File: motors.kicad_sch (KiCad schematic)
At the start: 0 parts

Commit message: Ajout des deux moteurs
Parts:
- added C12, C17: 1µF, Capacitor_SMD:C_0805_2012Metric, symbol local:C_0402
- added C13, C14, C16, C18: 10nF, Capacitor_SMD:C_0805_2012Metric, symbol local:C_0402
- added C15, C20: 1200µF, symbol Device:C_Polarized
- added J3, J4: B2B-XH-A_LF__SN_, local:JST_B2B-XH-A_LF__SN_, symbol local:B2B-XH-A_LF__SN_
- added R13, R16: 2.7k, symbol Device:R
- added R14, R15, R17, R18: 12, symbol Device:R
- added U3, U6: LMD18200, local:LMD18200, symbol local:LMD18200
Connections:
- new net: C13.1, U6.1 (BOOTSTRAP1)
- new net: C16.1, U6.11 (BOOTSTRAP2)
- new net: C14.1, U3.1 (BOOTSTRAP1)
- new net: C18.1, U3.11 (BOOTSTRAP2)
- new net CURRENT SENSE: R13.1, R16.1, U3.8 (CURRENT_SENSE_OUTPUT), U6.8 (CURRENT_SENSE_OUTPUT)
- new net Direction_MD: U3.3 (DIRECTION)
- new net Direction_MG: U6.3 (DIRECTION)
- new net GND: C12.1, C15.2, C17.1, C20.2, R13.2, R15.2, R16.2, R18.2, U3.4 (BRAKE), U3.7 (GND), U6.4 (BRAKE), U6.7 (GND)
- new net PWM_MD: U3.5 (PWM)
- new net PWM_MG: U6.5 (PWM)
- new net SINK_MD: C18.2, J3.2, R17.2, U3.10 (OUTPUT2)
- new net SINK_MG: C16.2, J4.2, R14.2, U6.10 (OUTPUT2)
- new net SOURCE_MD: C14.2, J3.1, R18.1, U3.2 (OUTPUT1)
- new net SOURCE_MG: C13.2, J4.1, R15.1, U6.2 (OUTPUT1)
- new net VS=42V: C12.2, C15.1, C17.2, C20.1, R14.1, R17.1, U3.6 (VS), U6.6 (VS)
- no-connect marks 0 -> 2

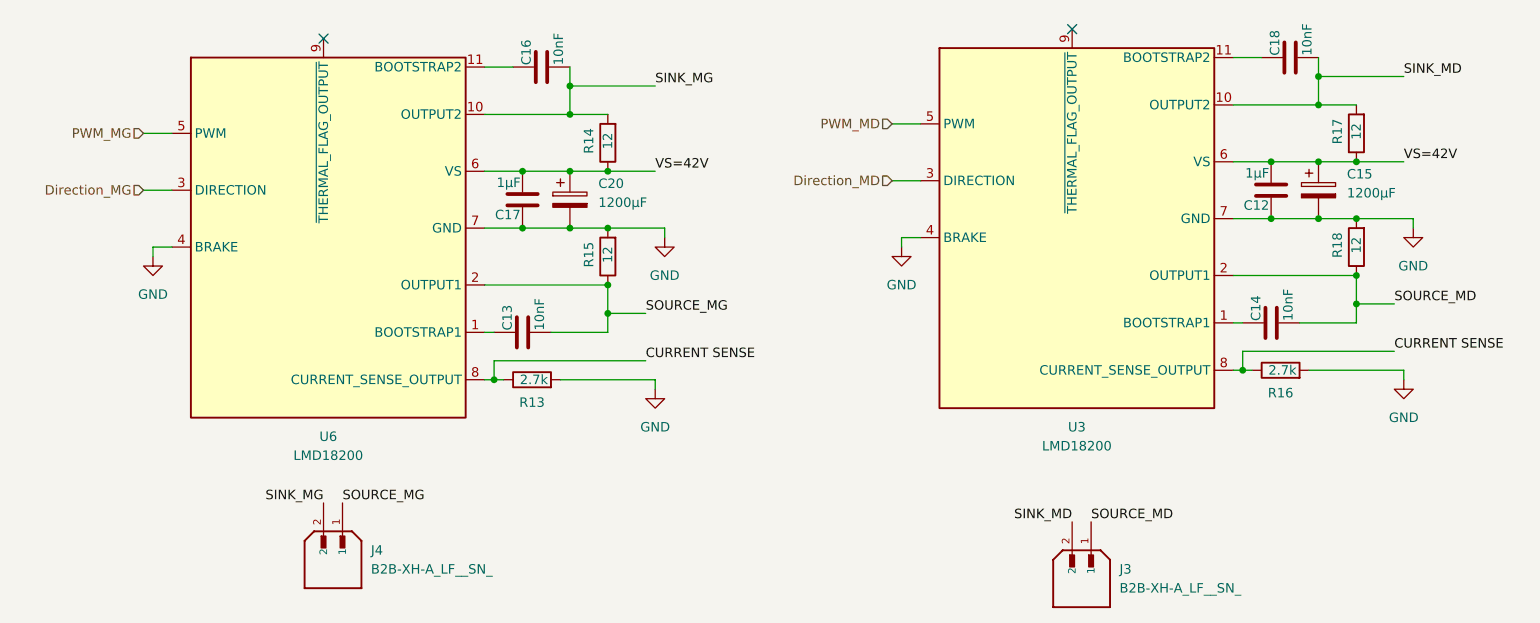
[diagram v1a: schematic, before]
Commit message: Version 0. Schémas finalisés. Mise à jour des résistances en série E12. Réduction de la BOM.
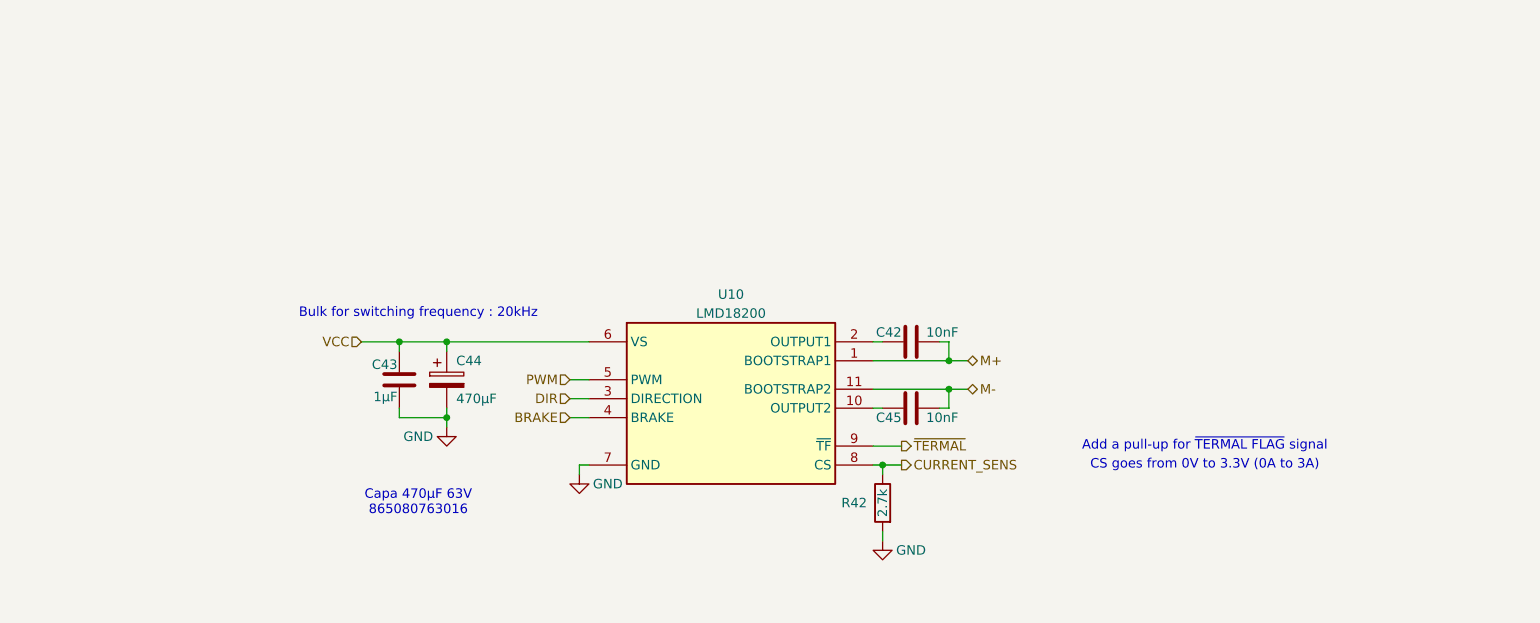
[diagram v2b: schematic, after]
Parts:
- removed C12, C17: 1µF, Capacitor_SMD:C_0805_2012Metric, symbol local:C_0402
- removed C13, C14, C16, C18: 10nF, Capacitor_SMD:C_0805_2012Metric, symbol local:C_0402
- removed C15, C20: 1200µF, symbol Device:C_Polarized
- removed J3, J4: B2B-XH-A_LF__SN_, local:JST_B2B-XH-A_LF__SN_, symbol local:B2B-XH-A_LF__SN_
- removed R13, R16: 2.7k, symbol Device:R
- removed R14, R15, R17, R18: 12, symbol Device:R
- removed U3: LMD18200, local:LMD18200, symbol local:LMD18200
- added C42, C45: 10nF, Capacitor_SMD:C_0805_2012Metric, symbol local:C_0402
- added C43: 1µF, Capacitor_SMD:C_0805_2012Metric, symbol local:C_0402
- added C44: 470µF, local:CP_Elec_16x17.5, symbol Device:C_Polarized
- added R42: 2.7k, Resistor_SMD:R_0805_2012Metric, symbol local:R
- renumbered U6 to U10
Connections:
- net GND: now also C43.2, C44.2, R42.2; no longer U10.4 (BRAKE)
- net M+: now reaches U10.1 (BOOTSTRAP1)
- net M+: now also C42.2
- net M-: now reaches U10.11 (BOOTSTRAP2)
- net M-: now also C45.2
- net ~{TERMAL}: now reaches U10.9 (~{TF})
- net CURRENT SENSE renamed CURRENT_SENS
- net CURRENT_SENS: now also R42.1
- net Direction_MG renamed DIR
- net PWM_MG renamed PWM
- net SINK_MG: no longer names the net of U10.10 (OUTPUT2)
- net SINK_MG: now also C45.1
- net SOURCE_MG: no longer names the net of U10.2 (OUTPUT1)
- net SOURCE_MG: now also C42.1
- net VS=42V renamed VCC
- net VCC: now also C43.1, C44.1
- new net BRAKE: U10.4 (BRAKE)
- no-connect marks 2 -> 0
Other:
- note added: "Add a pull-up for ~{TERMAL FLAG} signal"
- note added: "Bulk for switching frequency : 20kHz"
- note added: "CS goes from 0V to 3.3V (0A to 3A)"
- note added: "Capa 470µF 63V 865080763016"
- moved on the sheet: U10

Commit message: Minor Schematics update
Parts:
- C49: renamed from C42; footprint Capacitor_SMD:C_0805_2012Metric -> Capacitor_SMD:C_0603_1608Metric; symbol local:C_0402 -> local:C
- C50: renamed from C43; footprint Capacitor_SMD:C_0805_2012Metric -> Capacitor_SMD:C_0603_1608Metric; symbol local:C_0402 -> local:C
- C52: renamed from C45; footprint Capacitor_SMD:C_0805_2012Metric -> Capacitor_SMD:C_0603_1608Metric; symbol local:C_0402 -> local:C
- R54: renamed from R42; footprint Resistor_SMD:R_0805_2012Metric -> Resistor_SMD:R_0603_1608Metric
- renumbered C44 to C51
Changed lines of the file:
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@@
 		(on_board yes)
 		(dnp no)
-		(property "Reference" "C44"
+		(property "Reference" "C51"
 			(at 110.49 91.44 0)
 			(effects
@@
 			(project "tank"
 				(path "/7245ab6d-141f-4ee3-9edf-0ce22b32345b/739c4682-24b2-4c23-a05f-1c82de60687f"
-					(reference "C48")
-					(unit 1)
-				)
-				(path "/7245ab6d-141f-4ee3-9edf-0ce22b32345b/979e1608-c4e1-47fd-9792-1f8d0ad0fb1e"
-					(reference "C44")
+					(reference "C55")
+					(unit 1)
+				)
+				(path "/7245ab6d-141f-4ee3-9edf-0ce22b32345b/979e1608-c4e1-47fd-9792-1f8d0ad0fb1e"
+					(reference "C51")
 					(unit 1)
 				)
@@
 		(on_board yes)
 		(dnp no)
-		(property "Reference" "#PWR040"
+		(property "Reference" "#PWR047"
 			(at 127 113.03 0)
 			(effects
@@
 			(project "tank"
 				(path "/7245ab6d-141f-4ee3-9edf-0ce22b32345b/739c4682-24b2-4c23-a05f-1c82de60687f"
-					(reference "#PWR043")
-					(unit 1)
-				)
-				(path "/7245ab6d-141f-4ee3-9edf-0ce22b32345b/979e1608-c4e1-47fd-9792-1f8d0ad0fb1e"
-					(reference "#PWR040")
+					(reference "#PWR050")
+					(unit 1)
+				)
+				(path "/7245ab6d-141f-4ee3-9edf-0ce22b32345b/979e1608-c4e1-47fd-9792-1f8d0ad0fb1e"
+					(reference "#PWR047")
 					(unit 1)
 				)
@@
 		(on_board yes)
 		(dnp no)
-		(property "Reference" "#PWR039"
+		(property "Reference" "#PWR046"
 			(at 109.22 106.68 0)
 			(effects
@@
 			(project "tank"
 				(path "/7245ab6d-141f-4ee3-9edf-0ce22b32345b/739c4682-24b2-4c23-a05f-1c82de60687f"
-					(reference "#PWR042")
-					(unit 1)
-				)
-				(path "/7245ab6d-141f-4ee3-9edf-0ce22b32345b/979e1608-c4e1-47fd-9792-1f8d0ad0fb1e"
-					(reference "#PWR039")
+					(reference "#PWR049")
+					(unit 1)
+				)
+				(path "/7245ab6d-141f-4ee3-9edf-0ce22b32345b/979e1608-c4e1-47fd-9792-1f8d0ad0fb1e"
+					(reference "#PWR046")
 					(unit 1)
 				)
@@
 	)
 	(symbol
-		(lib_id "local:C_0402")
+		(lib_id "local:C")
 		(at 102.87 93.98 0)
 		(mirror y)
@@
 		(on_board yes)
 		(dnp no)
-		(property "Reference" "C43"
+		(property "Reference" "C50"
 			(at 102.616 91.948 0)
 			(effects
@@
 			)
 		)
-		(property "Footprint" "Capacitor_SMD:C_0805_2012Metric"
+		(property "Footprint" "Capacitor_SMD:C_0603_1608Metric"
 			(at 101.9048 97.79 0)
 			(effects
@@
 		)
 		(property "Description" "Unpolarized capacitor"
-			(at 107.696 93.726 90)
+			(at 102.87 93.98 0)
 			(effects
 				(font
@@
 			(project "tank"
 				(path "/7245ab6d-141f-4ee3-9edf-0ce22b32345b/739c4682-24b2-4c23-a05f-1c82de60687f"
-					(reference "C47")
-					(unit 1)
-				)
-				(path "/7245ab6d-141f-4ee3-9edf-0ce22b32345b/979e1608-c4e1-47fd-9792-1f8d0ad0fb1e"
-					(reference "C43")
+					(reference "C54")
+					(unit 1)
+				)
+				(path "/7245ab6d-141f-4ee3-9edf-0ce22b32345b/979e1608-c4e1-47fd-9792-1f8d0ad0fb1e"
+					(reference "C50")
 					(unit 1)
 				)
@@
 		(on_board yes)
 		(dnp no)
-		(property "Reference" "#PWR041"
+		(property "Reference" "#PWR048"
 			(at 167.64 121.92 0)
 			(effects
@@
 			(project "tank"
 				(path "/7245ab6d-141f-4ee3-9edf-0ce22b32345b/739c4682-24b2-4c23-a05f-1c82de60687f"
-					(reference "#PWR044")
-					(unit 1)
-				)
-				(path "/7245ab6d-141f-4ee3-9edf-0ce22b32345b/979e1608-c4e1-47fd-9792-1f8d0ad0fb1e"
-					(reference "#PWR041")
+					(reference "#PWR051")
+					(unit 1)
+				)
+				(path "/7245ab6d-141f-4ee3-9edf-0ce22b32345b/979e1608-c4e1-47fd-9792-1f8d0ad0fb1e"
+					(reference "#PWR048")
 					(unit 1)
 				)
@@
 		(on_board yes)
 		(dnp no)
-		(property "Reference" "R42"
+		(property "Reference" "R54"
 			(at 163.83 110.49 0)
 			(effects
@@
 			)
 		)
-		(property "Footprint" "Resistor_SMD:R_0805_2012Metric"
+		(property "Footprint" "Resistor_SMD:R_0603_1608Metric"
 			(at 169.418 110.49 90)
 			(effects
@@
 			(project "tank"
 				(path "/7245ab6d-141f-4ee3-9edf-0ce22b32345b/739c4682-24b2-4c23-a05f-1c82de60687f"
-					(reference "R43")
-					(unit 1)
-				)
-				(path "/7245ab6d-141f-4ee3-9edf-0ce22b32345b/979e1608-c4e1-47fd-9792-1f8d0ad0fb1e"
-					(reference "R42")
-					(unit 1)
-				)
-			)
-		)
-	)
-	(symbol
-		(lib_id "local:C_0402")
+					(reference "R55")
+					(unit 1)
+				)
+				(path "/7245ab6d-141f-4ee3-9edf-0ce22b32345b/979e1608-c4e1-47fd-9792-1f8d0ad0fb1e"
+					(reference "R54")
+					(unit 1)
+				)
+			)
+		)
+	)
+	(symbol
+		(lib_id "local:C")
 		(at 171.45 97.79 90)
 		(unit 1)
@@
 		(on_board yes)
 		(dnp no)
-		(property "Reference" "C45"
+		(property "Reference" "C52"
 			(at 170.18 99.06 90)
 			(effects
@@
 			)
 		)
-		(property "Footprint" "Capacitor_SMD:C_0805_2012Metric"
+		(property "Footprint" "Capacitor_SMD:C_0603_1608Metric"
 			(at 175.26 96.8248 0)
 			(effects
@@
 		)
 		(property "Description" "Unpolarized capacitor"
-			(at 171.196 102.616 90)
+			(at 171.45 97.79 0)
 			(effects
 				(font
@@
 			(project "tank"
 				(path "/7245ab6d-141f-4ee3-9edf-0ce22b32345b/739c4682-24b2-4c23-a05f-1c82de60687f"
-					(reference "C49")
-					(unit 1)
-				)
-				(path "/7245ab6d-141f-4ee3-9edf-0ce22b32345b/979e1608-c4e1-47fd-9792-1f8d0ad0fb1e"
-					(reference "C45")
-					(unit 1)
-				)
-			)
-		)
-	)
-	(symbol
-		(lib_id "local:C_0402")
+					(reference "C56")
+					(unit 1)
+				)
+				(path "/7245ab6d-141f-4ee3-9edf-0ce22b32345b/979e1608-c4e1-47fd-9792-1f8d0ad0fb1e"
+					(reference "C52")
+					(unit 1)
+				)
+			)
+		)
+	)
+	(symbol
+		(lib_id "local:C")
 		(at 171.45 88.9 90)
 		(unit 1)
@@
 		(on_board yes)
 		(dnp no)
-		(property "Reference" "C42"
+		(property "Reference" "C49"
 			(at 170.18 87.63 90)
 			(effects
@@
 			)
 		)
-		(property "Footprint" "Capacitor_SMD:C_0805_2012Metric"
+		(property "Footprint" "Capacitor_SMD:C_0603_1608Metric"
 			(at 175.26 87.9348 0)
 			(effects
@@
 		)
 		(property "Description" "Unpolarized capacitor"
-			(at 171.196 93.726 90)
+			(at 171.45 88.9 0)
 			(effects
 				(font
@@
 			(project "tank"
 				(path "/7245ab6d-141f-4ee3-9edf-0ce22b32345b/739c4682-24b2-4c23-a05f-1c82de60687f"
-					(reference "C46")
-					(unit 1)
-				)
-				(path "/7245ab6d-141f-4ee3-9edf-0ce22b32345b/979e1608-c4e1-47fd-9792-1f8d0ad0fb1e"
-					(reference "C42")
-					(unit 1)
-				)
+					(reference "C53")
+					(unit 1)
+				)
+				(path "/7245ab6d-141f-4ee3-9edf-0ce22b32345b/979e1608-c4e1-47fd-9792-1f8d0ad0fb1e"
+					(reference "C49")
+					(unit 1)
+				)
